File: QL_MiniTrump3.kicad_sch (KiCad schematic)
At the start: 25 parts, among them J1 QL_SLOT_DIN41612F, J2 Conn_02x17_Odd_Even, J3 QL_SLOT_DIN41612M, U1 GAL16V8, U14 27C128, U15 74HC04, U17 74LS175, U18 7805, X1 8Mhz

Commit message: Rev 2, with GAL code
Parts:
- added JP1: Jumper_2_Open, Jumper:SolderJumper-2_P1.3mm_Open_RoundedPad1.0x1.5mm, symbol Jumper:Jumper_2_Open
- D1, D6, D7, D8: footprint Diode_SMD:D_1206_3216Metric -> Diode_SMD:D_0805_2012Metric
- renumbered U to U13
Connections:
- net +5V: now also J1.a4 (SP0)
- net SP0: no longer J1.a4 (SP0)
- net AS: now reaches J3.b28 (~{AS})
- net AS: now also J1.b28 (~{AS})
- net at J1.b5 (~{BERR}): now also JP1.1 (A)
- net P13: now reaches U1.13 (IO7)
- net P13: now also JP1.2 (B)
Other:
- note added: "EXPANSION SIDE"
- note added: "NOTE: Use this jumper to allow a external memory expansion of +256Kb (for a total of 896Kb) to be used at same time."
- note added: "QL SIDE"
- moved on the sheet: C1, C10, C12, C13, C14, C15, C16, C2, C3, C4, D1, D6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

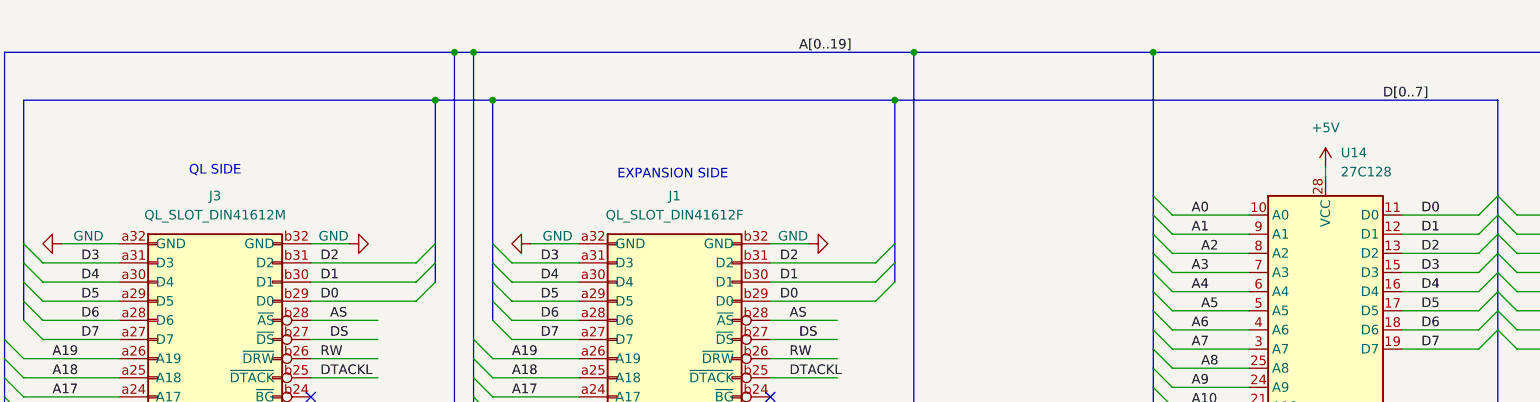
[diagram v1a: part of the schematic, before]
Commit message: fix eprom reference, shall be 27C256
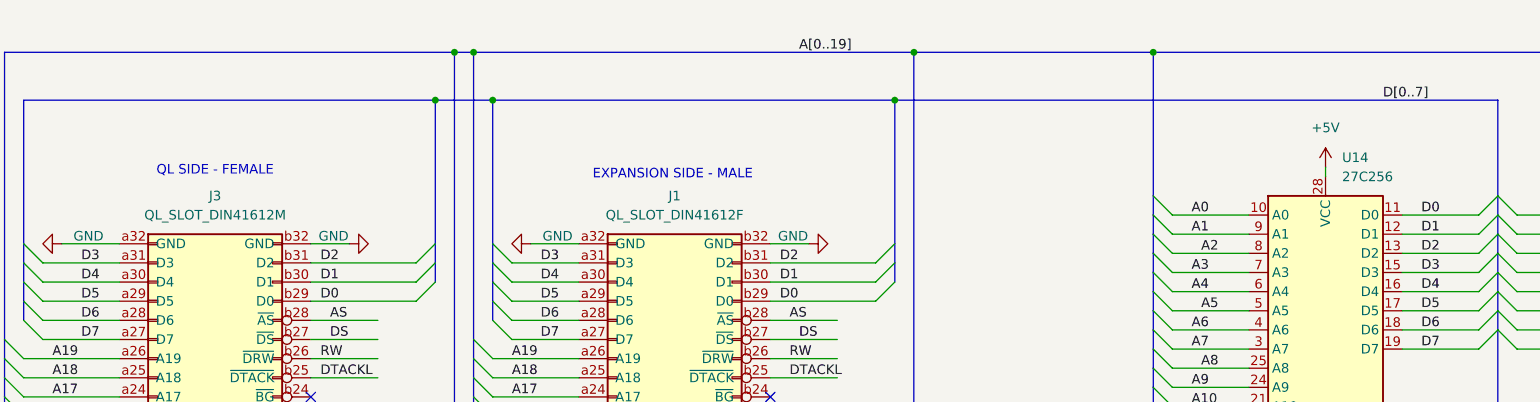
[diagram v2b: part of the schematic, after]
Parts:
- U14: value 27C128 -> 27C256
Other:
- note added: "EXPANSION SIDE - MALE"
- note added: "QL SIDE - FEMALE"
- note removed: "EXPANSION SIDE"
- note removed: "QL SIDE"
